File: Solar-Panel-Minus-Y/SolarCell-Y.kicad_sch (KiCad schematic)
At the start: 55 parts, among them IC2 TSL2561, J1 XF2M-1015-1A, J3 BATTERY CONNECTOR, J4 B2B-PH-SM4-TB_LF__SN_, U2 Value, U3 SW_SPDT, U4 SW_SPDT

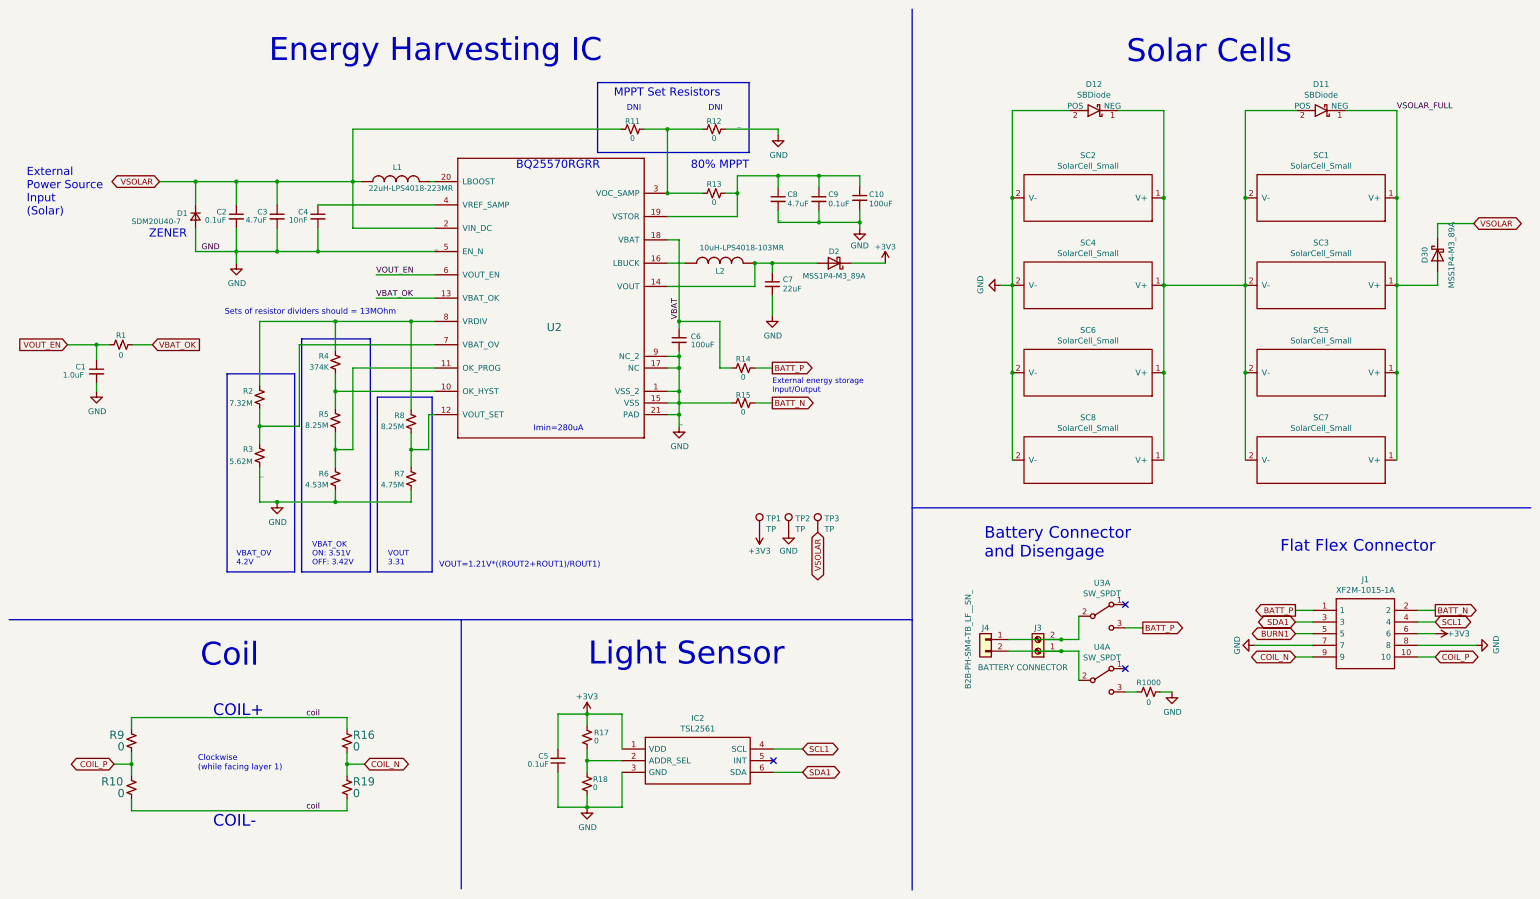
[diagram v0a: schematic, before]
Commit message: Added missing caps and fixed manufacturing error
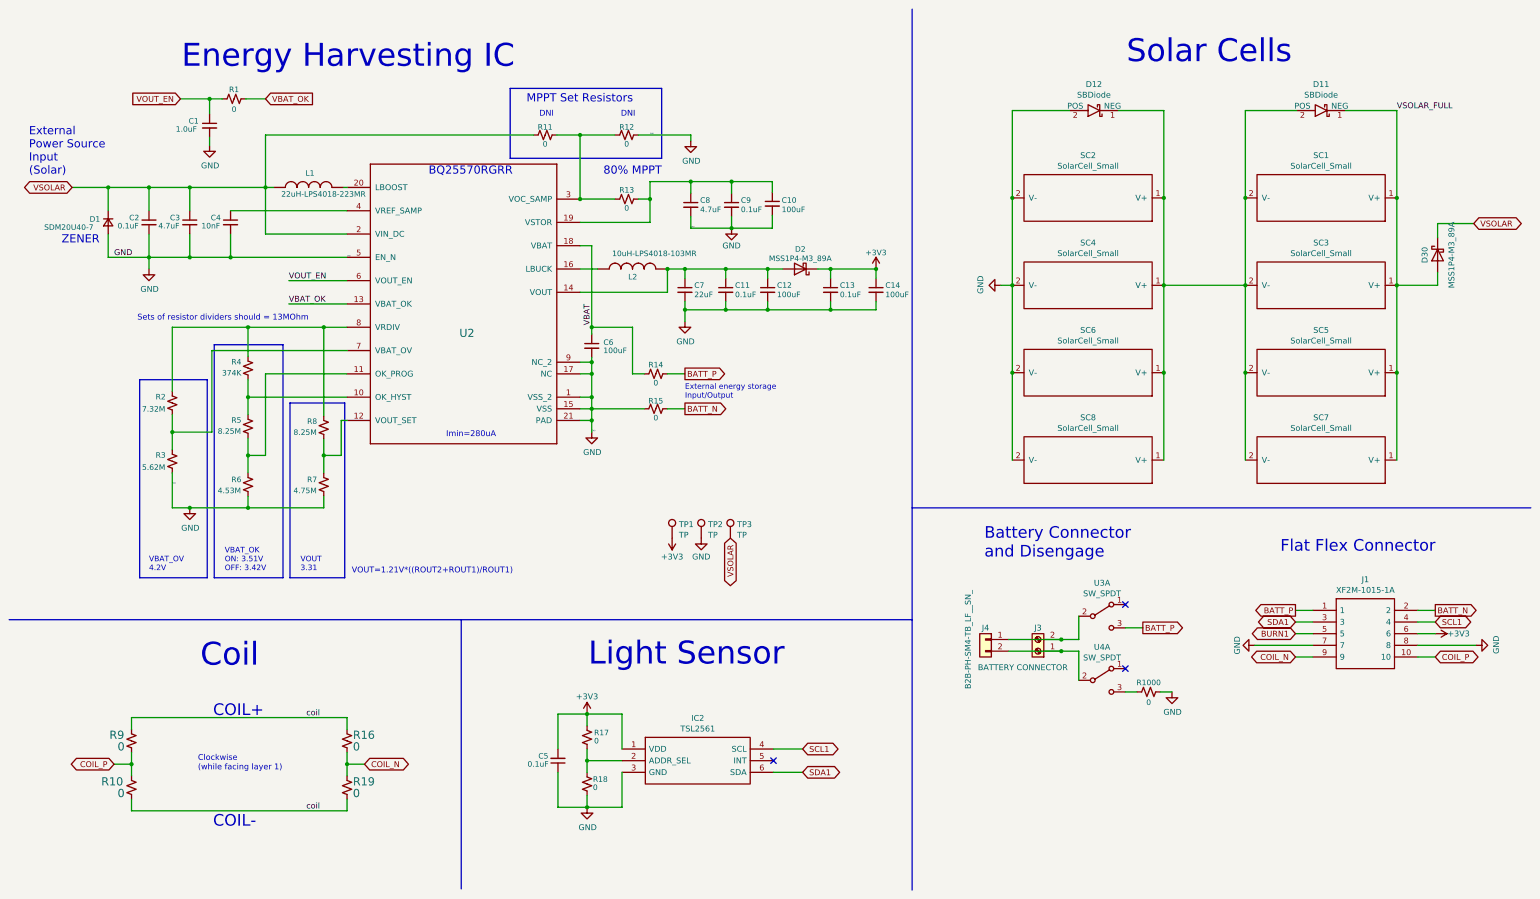
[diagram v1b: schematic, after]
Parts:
- added C11, C13: 0.1uF, Capacitor_SMD:C_0402_1005Metric, symbol Device:C_Small
- added C12, C14: 100uF, Capacitor_SMD:C_0402_1005Metric, symbol Device:C_Small
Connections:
- net +3V3: now also C13.1, C14.1
- net GND: now also C11.2, C12.2, C13.2, C14.2
- net at C7.1, D2.2 (A), L2.2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: now also C11.1, C12.1
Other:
- moved on the sheet: C1, C10, C2, C3, C4, C6, C7, C8, C9, D1, D2, L1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
